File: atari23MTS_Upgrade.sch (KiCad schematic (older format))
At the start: 40 parts, among them P1 CONN_01X01, P2 CONN_01X01, P3 CONN_01X01, P4 CONN_01X01, P5 CONN_01X01, P6 CONN_01X01, SW1 SW_PUSH, U1 NCP1117ST33T3G, U2 STM32F401RCTx, U3 74LS138

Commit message: Changed the bankselection $D530 and bankcontrol $D531
Changed the bankselection $D530 and bankcontrol $D531
Now in this way, only nCCTL can be used as address selector and only low
byte address is needed in the SoC
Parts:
- added R10: 2.2k, Resistors_SMD:R_1206_HandSoldering, symbol R_Small
- added R9: 10K, Resistors_SMD:R_1206_HandSoldering, symbol R_Small
- U1: symbol NCP1117ST33T3G -> NCP1117ST33T3G-RESCUE-atari23MTS_Upgrade
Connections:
- net GND: now also U1.1 (GND), R10.2
- net VCC3V3: now also R9.1
- net VCC5V: now also U1.3 (VI)
- net ~mRST: no longer U3.6 (E3)
- net at C2.1, C3.1, L2.2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: now also U1.2 (VO)
- net mA10: no longer names the net of U2.51 (PC10)
- net mA11: no longer names the net of U2.52 (PC11)
- net mA12: no longer names the net of U2.53 (PC12)
- net mA13: no longer names the net of U2.2 (PC13)
- net mA14: no longer names the net of U2.3 (PC14)
- net mA15: no longer names the net of U2.4 (PC15)
- net mA8 renamed RAMEN
- net RAMEN: now also U3.6 (E3), R10.1, R9.2
- net mA9: no longer names the net of U2.40 (PC9)
- no-connect marks 15 -> 22
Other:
- note added: "$D530 BANK SEL 0-255"
- note added: "$D531 BANK SEL ENABLE/DISABLE"
- moved on the sheet: U1

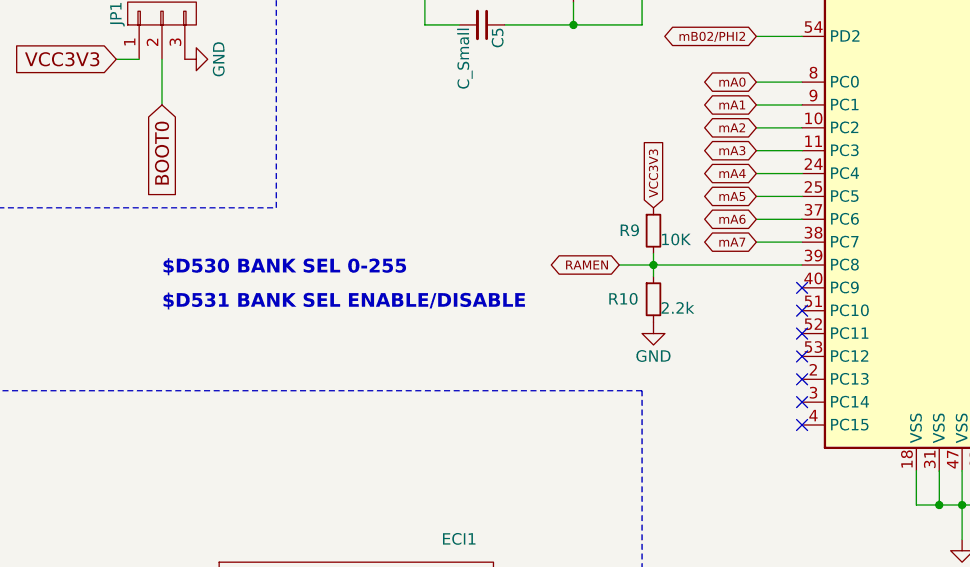
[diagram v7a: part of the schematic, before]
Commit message: Added D3xx selection logic for PIA (6520) if needed
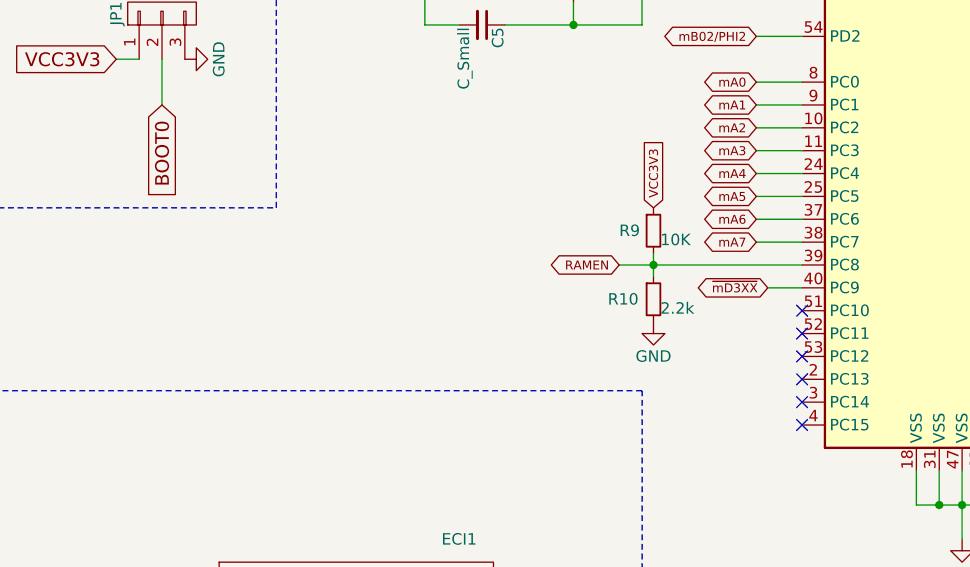
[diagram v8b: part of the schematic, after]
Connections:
- net ~mD3XX: now reaches U2.40 (PC9)
- no-connect marks 22 -> 21
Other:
- note removed: "$D530 BANK SEL 0-255"
- note removed: "$D531 BANK SEL ENABLE/DISABLE"
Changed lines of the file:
@@
 	6550 4500 6550 4600
 Connection ~ 6550 4550
-NoConn ~ 7200 4650
 NoConn ~ 7200 4750
 NoConn ~ 7200 4850
@@
 NoConn ~ 7200 5150
 NoConn ~ 7200 5250
-Text Notes 4400 4600 0    60   ~ 12
-$D530 BANK SEL 0-255
-Text Notes 4400 4750 0    60   ~ 12
-$D531 BANK SEL ENABLE/DISABLE
+Text GLabel 7050 4650 0    39   BiDi ~ 0
+~mD3XX
+Wire Wire Line
+	7200 4650 7050 4650
 $EndSCHEMATC
